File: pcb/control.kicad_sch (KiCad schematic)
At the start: 27 parts, among them J1 USB-C USB 2.0 MC-372, J2 Conn_01x04, J3 Conn_01x02, J4 Conn_01x04, J7 VIK_OUT, J8 VIK_OUT, Q1 AO3407, Q2 AO3407, U1 holyiot-18010-no-underside, U2 AP2112K-3.3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

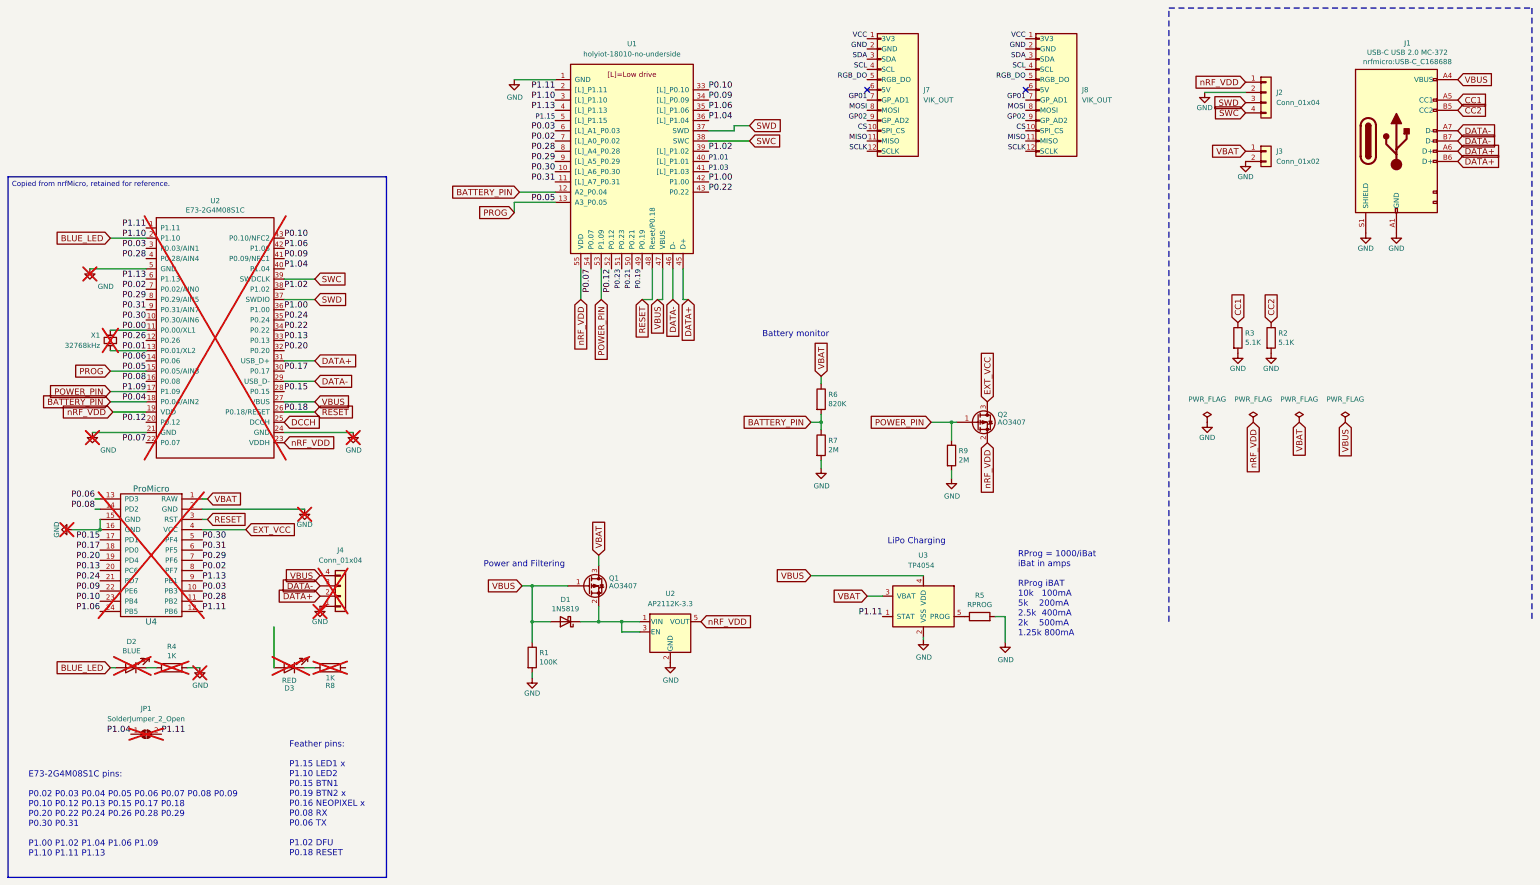
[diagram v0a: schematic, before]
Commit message: Complete preliminary PCB schematic.
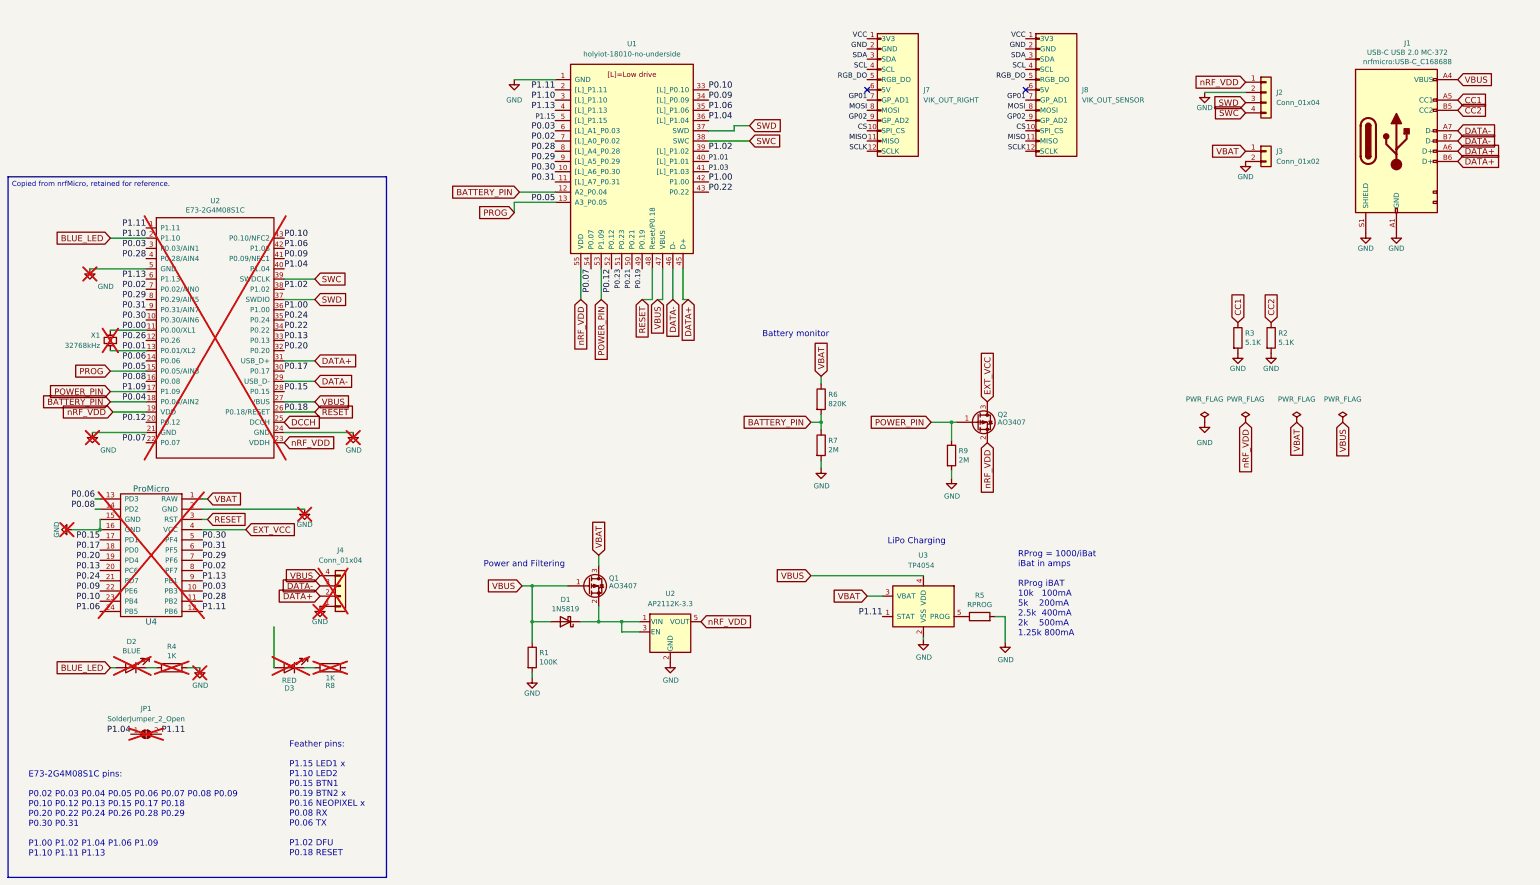
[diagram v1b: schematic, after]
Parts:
- J7: value VIK_OUT -> VIK_OUT_RIGHT
- J8: value VIK_OUT -> VIK_OUT_SENSOR
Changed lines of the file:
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@@
 	(generator "eeschema")
 	(generator_version "9.0")
-	(paper "A4")
+	(paper "A3")
 	(title_block
 		(title "Androphage Control")
@@
 		)
 	)
-	(polyline
-		(pts
-			(xy 280.67 12.7) (xy 280.67 165.1)
-		)
-		(stroke
-			(width 0)
-			(type dash)
-		)
-	)
 	(wire
 		(pts
@@
 		)
 	)
-	(polyline
-		(pts
-			(xy 190.5 165.1) (xy 190.5 12.7)
-		)
-		(stroke
-			(width 0)
-			(type dash)
-		)
-	)
 	(wire
 		(pts
@@
 		)
 	)
-	(polyline
-		(pts
-			(xy 190.5 12.7) (xy 280.67 12.7)
-		)
-		(stroke
-			(width 0)
-			(type dash)
-		)
-	)
 	(wire
 		(pts
@@
 	(global_label "VBAT"
 		(shape input)
-		(at 222.885 115.57 270)
+		(at 222.25 115.57 270)
 		(fields_autoplaced yes)
 		(effects
@@
 		)
 		(property "Intersheetrefs" "${INTERSHEET_REFS}"
-			(at 222.7898 123.6566 90)
+			(at 222.1548 123.6566 90)
 			(effects
 				(font
@@
 	(global_label "VBUS"
 		(shape input)
-		(at 234.315 115.57 270)
+		(at 233.68 115.57 270)
 		(fields_autoplaced yes)
 		(effects
@@
 		)
 		(property "Intersheetrefs" "${INTERSHEET_REFS}"
-			(at 234.2198 124.2372 90)
+			(at 233.5848 124.2372 90)
 			(effects
 				(font
@@
 	(global_label "nRF_VDD"
 		(shape input)
-		(at 211.455 115.57 270)
+		(at 209.55 115.57 270)
 		(fields_autoplaced yes)
 		(effects
@@
 		)
 		(property "Intersheetrefs" "${INTERSHEET_REFS}"
-			(at 211.3598 128.0835 90)
+			(at 209.4548 128.0835 90)
 			(effects
 				(font
@@
 			)
 		)
-		(property "Value" "VIK_OUT"
+		(property "Value" "VIK_OUT_SENSOR"
 			(at 168.91 35.5599 0)
 			(effects
@@
 	)
 	(symbol
+		(lib_name "GND_1")
+		(lib_id "power:GND")
+		(at 27.94 30.48 0)
+		(unit 1)
+		(exclude_from_sim no)
+		(in_bom yes)
+		(on_board yes)
+		(dnp no)
+		(fields_autoplaced yes)
+		(property "Reference" "#PWR02"
+			(at 27.94 36.83 0)
+			(effects
+				(font
+					(size 1.27 1.27)
+				)
+				(hide yes)
+			)
+		)
+		(property "Value" "GND"
+			(at 27.94 35.56 0)
+			(effects
+				(font
+					(size 1.27 1.27)
+				)
+			)
+		)
+		(property "Footprint" ""
+			(at 27.94 30.48 0)
+			(effects
+				(font
+					(size 1.27 1.27)
+				)
+				(hide yes)
+			)
+		)
+		(property "Datasheet" ""
+			(at 27.94 30.48 0)
+			(effects
+				(font
+					(size 1.27 1.27)
+				)
+				(hide yes)
+			)
+		)
+		(property "Description" "Power symbol creates a global label with name \"GND\" , ground"
+			(at 27.94 30.48 0)
+			(effects
+				(font
+					(size 1.27 1.27)
+				)
+				(hide yes)
+			)
+		)
+		(pin "1"
+		)
+		(instances
+			(project ""
+				(path "/99196bd8-ec0c-4029-b5c4-fcab8025953e/43544070-5b6a-4f5c-a637-418df5d67efe"
+					(reference "#PWR02")
+					(unit 1)
+				)
+			)
+		)
+	)
+	(symbol
 		(lib_id "nrfmicro-rescue:R")
 		(at -17.78 176.53 90)
@@
 			)
 		)
-		(property "Value" "VIK_OUT"
+		(property "Value" "VIK_OUT_RIGHT"
 			(at 129.54 35.5599 0)
 			(effects
@@
 	(symbol
 		(lib_id "power:PWR_FLAG")
-		(at 222.885 115.57 0)
+		(at 222.25 115.57 0)
 		(unit 1)
 		(exclude_from_sim no)
@@
 		(fields_autoplaced yes)
 		(property "Reference" "#FLG0101"
-			(at 222.885 113.665 0)
+			(at 222.25 113.665 0)
 			(effects
 				(font
@@
 		)
 		(property "Value" "PWR_FLAG"
-			(at 222.885 109.855 0)
+			(at 222.25 109.855 0)
 			(effects
 				(font
@@
 		)
 		(property "Footprint" ""
-			(at 222.885 115.57 0)
+			(at 222.25 115.57 0)
 			(effects
 				(font
@@
 		)
 		(property "Datasheet" "~"
-			(at 222.885 115.57 0)
+			(at 222.25 115.57 0)
 			(effects
 				(font
@@
 		)
 		(property "Description" ""
-			(at 222.885 115.57 0)
+			(at 222.25 115.57 0)
 			(effects
 				(font
@@
 	)
 	(symbol
-		(lib_id "nrfmicro-rescue:GND")
-		(at 200.025 115.57 0)
+		(lib_name "GND_1")
+		(lib_id "power:GND")
+		(at 199.39 115.57 0)
 		(unit 1)
 		(exclude_from_sim no)
@@
 		(on_board yes)
 		(dnp no)
-		(property "Reference" "#PWR0120"
-			(at 200.025 121.92 0)
+		(fields_autoplaced yes)
+		(property "Reference" "#PWR01"
+			(at 199.39 121.92 0)
 			(effects
 				(font
@@
 		)
 		(property "Value" "GND"
-			(at 200.025 119.38 0)
+			(at 199.39 120.65 0)
 			(effects
 				(font
@@
 		)
 		(property "Footprint" ""
-			(at 200.025 115.57 0)
+			(at 199.39 115.57 0)
 			(effects
 				(font
@@
 		)
 		(property "Datasheet" ""
-			(at 200.025 115.57 0)
+			(at 199.39 115.57 0)
 			(effects
 				(font
@@
 			)
 		)
-		(property "Description" ""
-			(at 200.025 115.57 0)
+		(property "Description" "Power symbol creates a global label with name \"GND\" , ground"
+			(at 199.39 115.57 0)
 			(effects
 				(font
 					(size 1.27 1.27)
 				)
+				(hide yes)
 			)
 		)
@@
 			(project "androphage"
 				(path "/99196bd8-ec0c-4029-b5c4-fcab8025953e/43544070-5b6a-4f5c-a637-418df5d67efe"
-					(reference "#PWR0120")
+					(reference "#PWR01")
 					(unit 1)
 				)
@@
 	(symbol
 		(lib_id "power:PWR_FLAG")
-		(at 200.025 115.57 0)
+		(at 199.39 115.57 0)
 		(unit 1)
 		(exclude_from_sim no)
@@
 		(fields_autoplaced yes)
 		(property "Reference" "#FLG0103"
-			(at 200.025 113.665 0)
+			(at 199.39 113.665 0)
 			(effects
 				(font
@@
 		)
 		(property "Value" "PWR_FLAG"
-			(at 200.025 109.855 0)
+			(at 199.39 109.855 0)
 			(effects
 				(font
@@
 		)
 		(property "Footprint" ""
-			(at 200.025 115.57 0)
+			(at 199.39 115.57 0)
 			(effects
 				(font
@@
 		)
 		(property "Datasheet" "~"
-			(at 200.025 115.57 0)
+			(at 199.39 115.57 0)
 			(effects
 				(font
@@
 		)
 		(property "Description" ""
-			(at 200.025 115.57 0)
+			(at 199.39 115.57 0)
 			(effects
 				(font
@@
 	(symbol
 		(lib_id "power:PWR_FLAG")
-		(at 211.455 115.57 0)
+		(at 209.55 115.57 0)
 		(unit 1)
 		(exclude_from_sim no)
@@
 		(fields_autoplaced yes)
 		(property "Reference" "#FLG0104"
-			(at 211.455 113.665 0)
+			(at 209.55 113.665 0)
 			(effects
 				(font
@@
 		)
 		(property "Value" "PWR_FLAG"
-			(at 211.455 109.855 0)
+			(at 209.55 109.855 0)
 			(effects
 				(font
@@
 		)
 		(property "Footprint" ""
-			(at 211.455 115.57 0)
+			(at 209.55 115.57 0)
 			(effects
 				(font
@@
 		)
 		(property "Datasheet" "~"
-			(at 211.455 115.57 0)
+			(at 209.55 115.57 0)
 			(effects
 				(font
@@
 		)
 		(property "Description" ""
-			(at 211.455 115.57 0)
+			(at 209.55 115.57 0)
 			(effects
 				(font
@@
 	(symbol
 		(lib_id "power:PWR_FLAG")
-		(at 234.315 115.57 0)
+		(at 233.68 115.57 0)
 		(unit 1)
 		(exclude_from_sim no)
@@
 		(fields_autoplaced yes)
 		(property "Reference" "#FLG0102"
-			(at 234.315 113.665 0)
+			(at 233.68 113.665 0)
 			(effects
 				(font
@@
 		)
 		(property "Value" "PWR_FLAG"
-			(at 234.315 109.855 0)
+			(at 233.68 109.855 0)
 			(effects
 				(font
@@
 		)
 		(property "Footprint" ""
-			(at 234.315 115.57 0)
+			(at 233.68 115.57 0)
 			(effects
 				(font
@@
 		)
 		(property "Datasheet" "~"
-			(at 234.315 115.57 0)
+			(at 233.68 115.57 0)
 			(effects
 				(font
@@
 		)
 		(property "Description" ""
-			(at 234.315 115.57 0)
+			(at 233.68 115.57 0)
 			(effects
 				(font
@@
 					(unit 1)
 				)
-			)
-		)
-	)
-	(symbol
-		(lib_id "power:GND")
-		(at 27.94 30.48 0)
-		(unit 1)
-		(exclude_from_sim no)
-		(in_bom yes)
-		(on_board yes)
-		(dnp no)
-		(property "Reference" "#PWR01"
-			(at 27.94 36.83 0)
-			(effects
-				(font
-					(size 1.27 1.27)
-				)
-				(hide yes)
-			)
-		)
-		(property "Value" "GND"
-			(at 28.067 34.8742 0)
-			(effects
-				(font
-					(size 1.27 1.27)
-				)
-			)
-		)
-		(property "Footprint" ""
-			(at 27.94 30.48 0)
-			(effects
-				(font
-					(size 1.27 1.27)
-				)
-				(hide yes)
-			)
-		)
-		(property "Datasheet" ""
-			(at 27.94 30.48 0)
-			(effects
-				(font
-					(size 1.27 1.27)
-				)
-				(hide yes)
-			)
-		)
-		(property "Description" ""
-			(at 27.94 30.48 0)
-			(effects
-				(font
-					(size 1.27 1.27)
-				)
-			)
-		)
-		(pin "1"
-		)
-		(instances
-			(project "androphage"
-				(path "/99196bd8-ec0c-4029-b5c4-fcab8025953e/43544070-5b6a-4f5c-a637-418df5d67efe"
-					(reference "#PWR01")
-					(unit 1)
-				)
